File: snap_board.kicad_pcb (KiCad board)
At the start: 6 copper layers, 121 parts, among them U1 STM32MP157CAC3, U2 AS4C256M16D3LC-12BCN, U3 S40FC004C1B2C00000, U4 STPMIC1BPQR, U5 DF40C-70DP-0.4V(51), U6 DF40C-70DP-0.4V(51), U7 DF40C-70DP-0.4V(51), X1 32.768kHz, X2 24MHz

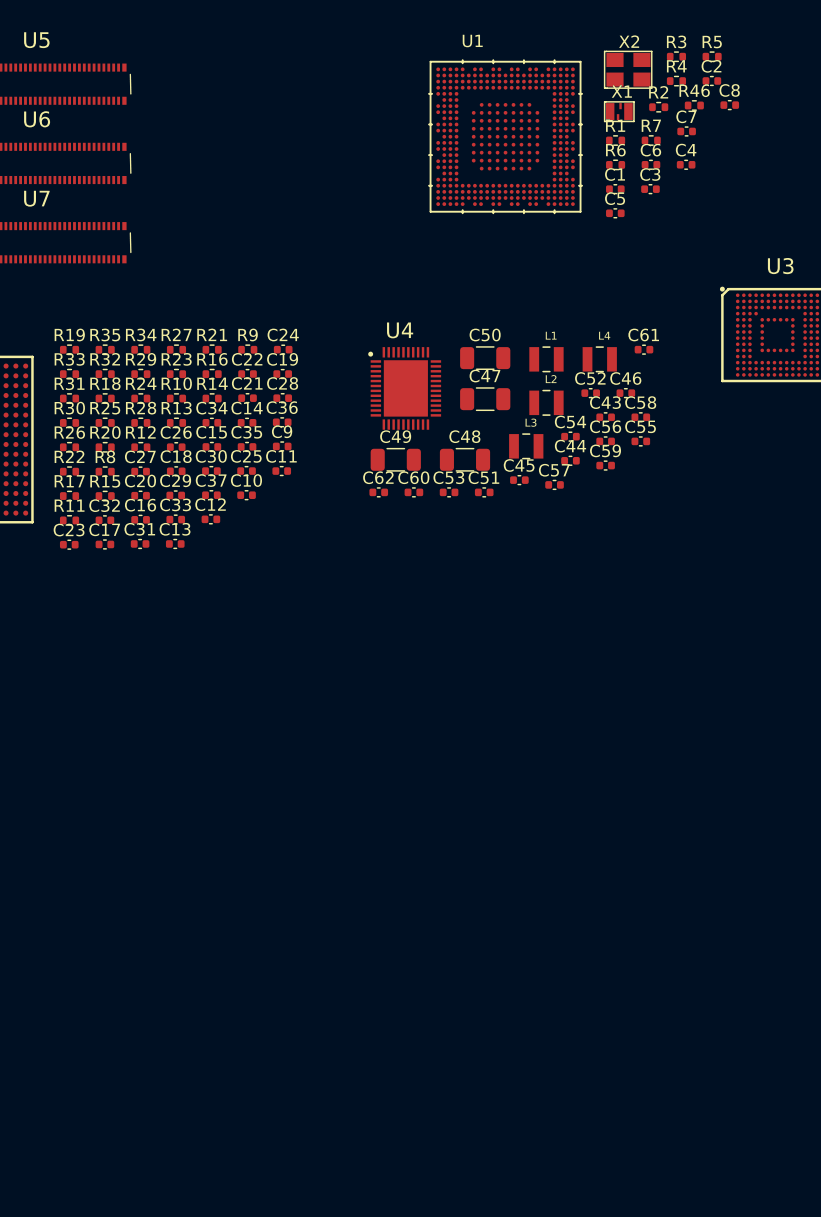
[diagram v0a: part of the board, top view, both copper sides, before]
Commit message: updated stm32 footprint
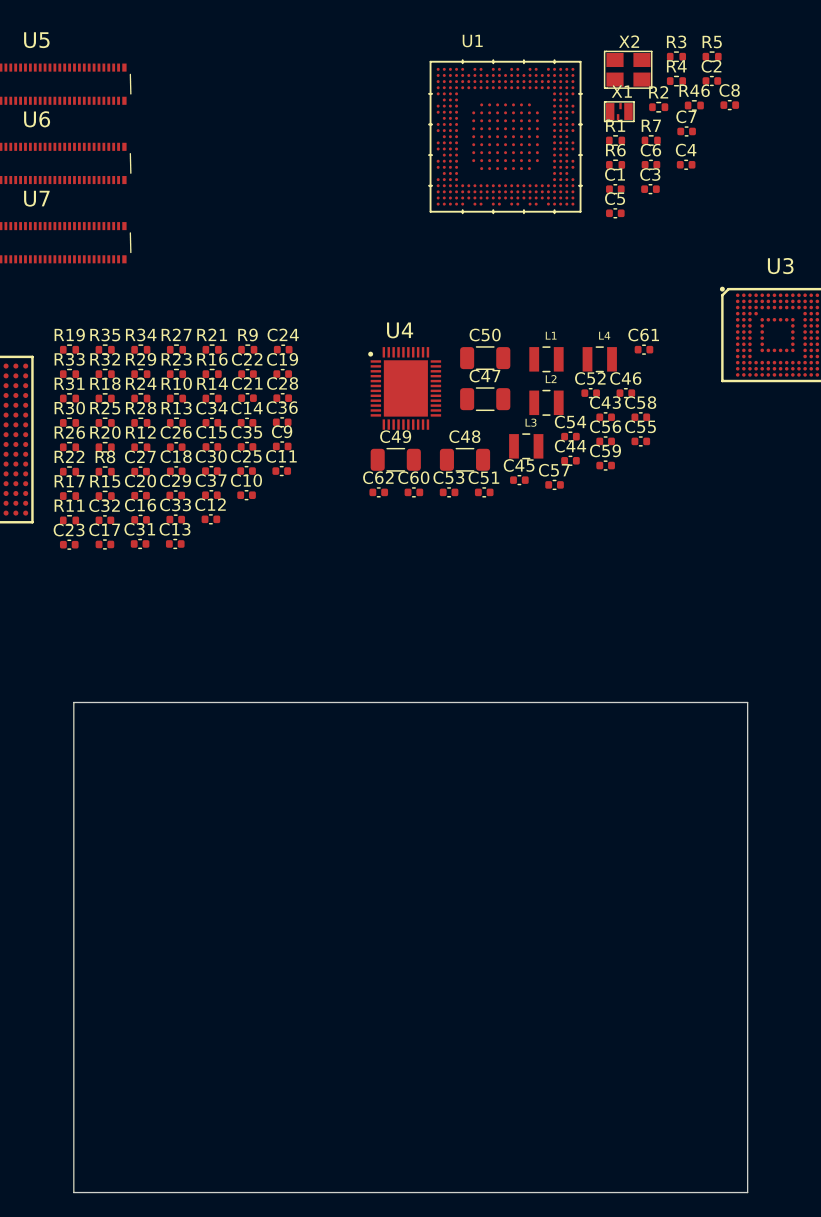
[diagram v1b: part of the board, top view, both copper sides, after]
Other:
- board outline added: 55 x 40 mm
- net class Default: clearance 0.2 -> 0.08; trace_width 0.25 -> 0.09; via_dia 0.8 -> 0.4; via_drill 0.4 -> 0.2
- rule trace_clearance: 0.2 -> 0.08
- rule trace_min: 0.2 -> 0.09
- rule via_min_drill: 0.3 -> 0.2

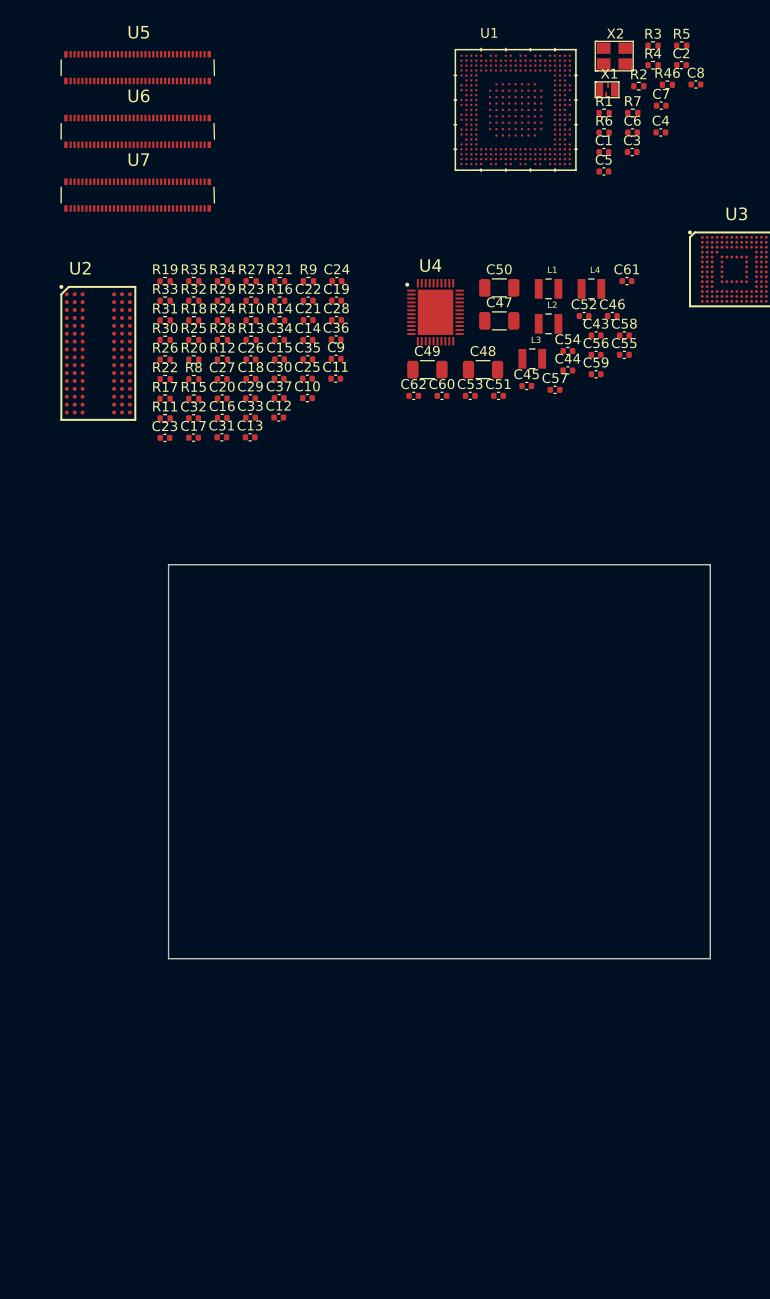
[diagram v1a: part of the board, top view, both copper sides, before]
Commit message: working on bga fanout
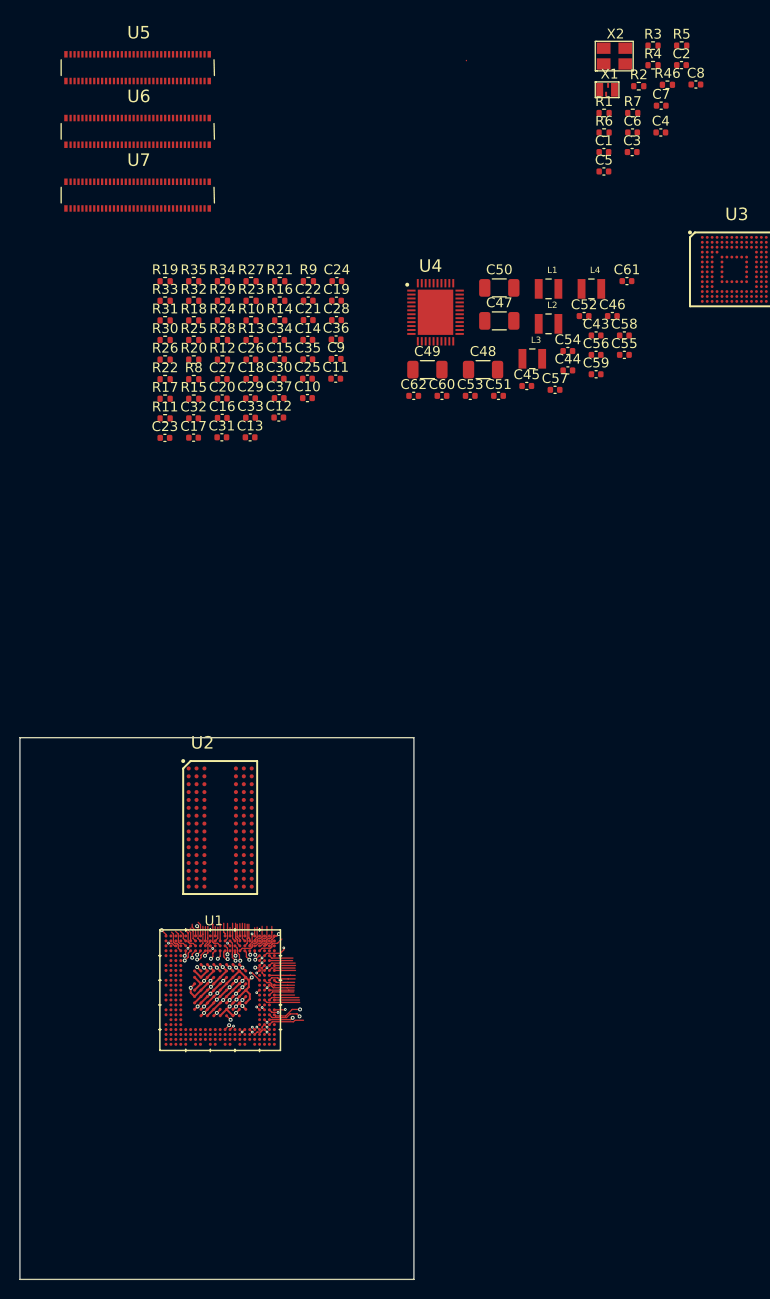
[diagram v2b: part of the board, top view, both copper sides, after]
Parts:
- moved U1 94.3 mm to (205.7, 148.6)
- moved U2 49.7 mm to (205.7, 132.1)
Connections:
- net DDR_DQS1N renamed DDR_DQS1_N
- net DDR_DQS1P renamed DDR_DQS1_P
- U1 pad 1E5: (no net) -> GND
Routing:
- net GND: track 0.00 -> 55.9 mm, vias 0 -> 19
- net PMIC_VOUT1_VDD_CORE: track 0.00 -> 18.3 mm, vias 0 -> 11
- net PMIC_VOUT3_VDD: track 0.00 -> 8.86 mm, vias 0 -> 8
- net SDMMC1_D3: track 0.00 -> 4.19 mm
- net Net-(C5-Pad2): track 0.00 -> 3.65 mm, vias 0 -> 1
- net DDR_DQ14: track 0.00 -> 3.64 mm
- net DDR_DQS1_P: track 0.00 -> 3.44 mm, vias 0 -> 1
- net DDR_A1: track 0.00 -> 3.11 mm
- net DDR_DQS1_N: track 0.00 -> 3.03 mm, vias 0 -> 1
- net DDR_RESETN: track 0.00 -> 2.90 mm
- net JTMS_SWDIO: track 0.00 -> 2.84 mm
- net Net-(U1-PadC19): track 0.00 -> 2.84 mm
- net DDR_A3: track 0.00 -> 2.76 mm
- net DDR_DQS0_P: track 0.00 -> 2.72 mm
- net DDR_DQ6: track 0.00 -> 2.71 mm
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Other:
- board size 55 x 40 mm -> 40 x 55 mm
- net class DDR_DiffPairs added: clearance 0.08, trace_width 0.09, via_dia 0.4, via_drill 0.2

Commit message: working on PCB
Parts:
- moved C61 126.4 mm to (141.3, 145.9), turned to 180 degrees
- moved C46 123.8 mm to (141.3, 146.9), turned to 180 degrees
- moved C58 120.4 mm to (141.4, 140.2), turned to 180 degrees
- moved C55 119.9 mm to (141.4, 141.2), turned to 180 degrees
- moved L4 119.0 mm to (147.0, 147.2), turned to 270 degrees
- moved C52 117.9 mm to (145.2, 146.5), turned to 270 degrees
- moved C56 117.7 mm to (144.1, 146.5), turned to 270 degrees
- moved C50 115.8 mm to (143.3, 149.2), turned to 180 degrees
- moved C54 114.0 mm to (141.4, 139.1), turned to 180 degrees
- moved C57 112.7 mm to (141.3, 142.6), turned to 180 degrees
- moved C44 112.5 mm to (141.4, 137.9), turned to 180 degrees
- moved C43 111.1 mm to (146.4, 135.4), turned to 90 degrees
- moved C45 111.0 mm to (141.3, 143.8), turned to 180 degrees
- moved L2 109.4 mm to (144.3, 135.5), turned to 90 degrees
- moved L1 107.6 mm to (148.9, 136.1)
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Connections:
- C57 pad 1: PMIC_LDO2_2V5 -> PMIC_LDO2_2V9
- U4 pad 11: PMIC_VOUT2_VDD_DDR -> Net-(L2-Pad1)
- U4 pad 5: Net-(L1-Pad1) -> PMIC_VOUT1_VDD_CORE
- U4 pad 7: PMIC_VOUT1_VDD_CORE -> Net-(L1-Pad1)
- U4 pad 9: Net-(L2-Pad1) -> PMIC_VOUT2_VDD_DDR
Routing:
- net GND: track 55.9 -> 82.4 mm, vias 19 -> 58
- net 5V_VIN: track 0.00 -> 11.1 mm, vias 0 -> 11
- net PMIC_VOUT2_VDD_DDR: track 1.84 -> 11.8 mm, vias 2 -> 10
- net PMIC_VOUT3_VDD: track 8.86 -> 16.9 mm, vias 8 -> 10
- net I2C4_SCL: track 0.00 -> 6.85 mm
- net I2C4_SDA: track 0.00 -> 6.10 mm
- net PMIC_WAKEUP: track 0.00 -> 5.54 mm
- net NRST: track 0.00 -> 5.31 mm
- net PMIC_LDO6_1V0: track 0.00 -> 4.89 mm
- net PMIC_LDO2_2V9: track 0.00 -> 4.82 mm, vias 0 -> 1
- net PMIC_LDO5: track 0.00 -> 4.33 mm
- net LCD_G5: track 0.00 -> 4.25 mm
- net PA0_WKUP: track 0.00 -> 4.21 mm
- net ETH_GTX_CLK: track 0.00 -> 4.18 mm
- net LCD_R0: track 0.00 -> 4.13 mm
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- added copper zone on F.Cu, net 5V_VIN
- added copper zone on F.Cu, net Net-(L1-Pad1)
- added copper zone on F.Cu, net Net-(L2-Pad1)
- added copper zone on F.Cu, net Net-(L3-Pad1)
- added copper zone on F.Cu, net Net-(L4-Pad1)
- added copper zone on F.Cu, net PMIC_LDO3_VTT_DDR
- added copper zone on F.Cu, net PMIC_VOUT1_VDD_CORE
- added copper zone on F.Cu, net PMIC_VOUT2_VDD_DDR
- added copper zone on F.Cu, net PMIC_VOUT3_VDD
- added copper zone on F.Cu, net PMIC_VOUT4_3V3

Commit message: working on RAM
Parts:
- R10, R11, R8, R9: moved to B.Cu
- moved R5 137.8 mm to (138.3, 129.7), turned to 270 degrees
- moved R46 135.5 mm to (138.3, 131.7), turned to 270 degrees
- moved R4 135.2 mm to (137.3, 129.7), turned to 270 degrees
- moved C59 116.8 mm to (137.9, 135.0)
- moved C51 107.4 mm to (137.9, 136.2)
- moved C62 98.6 mm to (137.9, 133.8)
- moved R9 77.5 mm to (143.7, 107.9), turned to 180 degrees
- moved R10 71.6 mm to (143.7, 110.2)
- moved R8 63.4 mm to (143.7, 109.0)
- moved U2 61.2 mm to (150.6, 105.4)
- moved U1 55.7 mm to (150.2, 152.6)
- moved R11 45.3 mm to (159.5, 110.5)
- moved C13 41.2 mm to (173.4, 113.5)
- moved C24 41.2 mm to (182.2, 97.7)
- moved C34 41.2 mm to (176.4, 103.7)
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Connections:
- C51 pad 1: PMIC_VOUT4_3V3 -> 5V_VIN
- U2 pad A2: DDR_DQ13 -> DDR_DQ0
- U2 pad A3: DDR_DQ15 -> DDR_DQ7
- U2 pad A7: DDR_DQ12 -> DDR_DQ2
- U2 pad B7: DDR_DQS1_P -> DDR_DQS0_N
- U2 pad B8: DDR_DQ14 -> DDR_DQ4
- U2 pad C2: DDR_DQ11 -> DDR_DQ3
- U2 pad C3: DDR_DQ9 -> DDR_DQ1
- U2 pad C7: DDR_DQS1_N -> DDR_DQS0_P
- U2 pad C8: DDR_DQ10 -> DDR_DQ5
- U2 pad D3: DDR_DQM1 -> DDR_DQM0
- U2 pad D7: DDR_DQ8 -> DDR_DQ6
- U2 pad E3: DDR_DQ0 -> DDR_DQ9
- U2 pad E7: DDR_DQM0 -> DDR_DQM1
- U2 pad F2: DDR_DQ2 -> DDR_DQ8
- U2 pad F3: DDR_DQS0_N -> DDR_DQS1_P
- U2 pad F7: DDR_DQ1 -> DDR_DQ11
- U2 pad F8: DDR_DQ3 -> DDR_DQ15
- U2 pad G2: DDR_DQ6 -> DDR_DQ10
- U2 pad G3: DDR_DQS0_P -> DDR_DQS1_N
- U2 pad H3: DDR_DQ4 -> DDR_DQ13
- U2 pad H7: DDR_DQ7 -> DDR_DQ14
- U2 pad H8: DDR_DQ5 -> DDR_DQ12
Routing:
- net GND: track 82.4 -> 104.8 mm, vias 58 -> 82
- net PMIC_VOUT2_VDD_DDR: track 11.8 -> 32.5 mm, vias 10 -> 22
- net PA0_WKUP: track 4.21 -> 8.31 mm
- net POWER_ON: track 2.07 -> 6.09 mm
- net PMIC_VOUT3_VDD: track 16.9 -> 20.6 mm, vias 10 -> 12
- net I2C4_SDA: track 6.10 -> 9.31 mm
- net PMIC_WAKEUP: track 5.54 -> 2.41 mm
- net PMIC_VREF_DDR: track 2.43 -> 5.26 mm, vias 0 -> 2
- net DDR_RESETN: track 3.36 -> 5.80 mm, vias 0 -> 1
- net Net-(C62-Pad1): track 0.00 -> 2.15 mm
- net I2C4_SCL: track 6.85 -> 8.82 mm
- net DDR_A13: track 1.20 -> 3.17 mm, vias 1 -> 2
- net DDR_A4: track 0.43 -> 2.07 mm, vias 1 -> 2
- net DDR_A8: track 2.90 -> 4.49 mm, vias 0 -> 1
- net DDR_A11: track 0.53 -> 2.09 mm, vias 1 -> 2
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- added copper zone on F.Cu, net PMIC_LDO4_VDD_USB
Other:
- board outline removed

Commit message: working on RAM
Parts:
- moved R1 128.7 mm to (147.8, 144.2), turned to 180 degrees
- moved R27 54.0 mm to (145.0, 143.6), turned to 180 degrees
- moved C24 47.4 mm to (156.9, 137.7), turned to 270 degrees
- moved C36 40.9 mm to (156.9, 135.7), turned to 90 degrees
- moved R34 38.5 mm to (156.8, 133.7), turned to 90 degrees
- moved C43 38.0 mm to (94.1, 129.1)
- moved C47 38.0 mm to (96.9, 127.2)
- moved C50 38.0 mm to (90.9, 142.9)
- moved L1 38.0 mm to (96.6, 129.9)
- moved R4 38.0 mm to (99.3, 130.2)
- moved R46 38.0 mm to (100.4, 132.1)
- moved C44 38.0 mm to (89.0, 131.7)
- moved C45 38.0 mm to (89.0, 137.6)
- moved C46 38.0 mm to (89.0, 140.7)
- moved C48 38.0 mm to (88.2, 128.4)
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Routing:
- net DDR_DQ12: track 0.83 -> 25.4 mm
- net DDR_DQS1_P: track 1.89 -> 26.0 mm
- net DDR_DQS1_N: track 1.29 -> 25.1 mm
- net DDR_DQM1: track 1.78 -> 24.9 mm
- net DDR_DQ9: track 2.29 -> 25.0 mm
- net DDR_DQ11: track 2.84 -> 25.0 mm
- net DDR_DQ13: track 1.25 -> 23.1 mm
- net DDR_DQ15: track 2.84 -> 24.6 mm
- net DDR_DQ8: track 2.47 -> 24.2 mm
- net DDR_DQ10: track 1.80 -> 23.5 mm
- net DDR_DQ14: track 1.49 -> 22.8 mm
- net GND: track 104.8 -> 113.7 mm, vias 82 -> 84
- net DDR_CSN: track 2.31 -> 11.1 mm, vias 1 -> 2
- net DDR_CKE: track 4.79 -> 12.5 mm, vias 1 -> 2
- net PMIC_VOUT2_VDD_DDR: track 32.5 -> 39.7 mm
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
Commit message: still working on RAM
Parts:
- C10, C11, C12, C13, C14, C15, C16, C17, C18, C19, C20, C21, C22, C30, C31, C32, C33, C9, R12, R13, R14, R15, R17, R18, R19, R20, R21, R22, R23, R24, R25, R26, R28, R29, R30, R31, R32, R33, R35: moved to B.Cu
- Re: renamed from R16; moved to B.Cu
- moved R21 51.0 mm to (145.2, 138.1)
- moved C11 48.5 mm to (143.2, 136.5), turned to 180 degrees
- moved R9 48.4 mm to (158.5, 129.9)
- moved C10 46.3 mm to (143.2, 138.6), turned to 180 degrees
- moved C28 46.0 mm to (145.8, 129.7), turned to 270 degrees
- moved C14 44.7 mm to (143.2, 129.9), turned to 180 degrees
- moved Re 43.3 mm to (158.4, 139.0), turned to 180 degrees
- moved R10 42.9 mm to (145.2, 134.8)
- moved R13 42.9 mm to (145.2, 135.9)
- moved R23 42.6 mm to (145.2, 131.6)
- moved C19 42.6 mm to (160.5, 136.3)
- moved R8 42.0 mm to (145.2, 132.6)
- moved R14 40.5 mm to (158.4, 137.9), turned to 180 degrees
- moved C12 40.2 mm to (143.2, 134.3), turned to 180 degrees
- moved C35 40.2 mm to (145.8, 127.7), turned to 270 degrees
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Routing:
- net DDR_CASN: track 1.73 -> 22.7 mm
- net DDR_RASN: track 1.54 -> 22.3 mm
- net DDR_WEN: track 1.48 -> 20.5 mm
- net DDR_ODT: track 5.37 -> 23.3 mm
- net DDR_CSN: track 11.1 -> 22.0 mm
- net GND: track 113.7 -> 122.4 mm, vias 84 -> 85
- net PMIC_VOUT2_VDD_DDR: track 39.7 -> 45.6 mm
- net DDR_DQ8: track 24.2 -> 26.1 mm
- net DDR_DQ10: track 23.5 -> 25.4 mm
- net PMIC_VREF_DDR: track 6.68 -> 8.37 mm

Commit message: still working on RAM
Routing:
- net DDR_A12: track 2.06 -> 25.9 mm
- net DDR_CLK_P: track 3.33 -> 26.7 mm
- net DDR_CLK_N: track 2.94 -> 25.8 mm
- net DDR_A0: track 1.58 -> 24.3 mm
- net DDR_A3: track 2.31 -> 24.7 mm
- net DDR_A5: track 1.10 -> 23.5 mm
- net DDR_A9: track 2.22 -> 23.9 mm
- net DDR_A2: track 1.95 -> 23.4 mm
- net DDR_A1: track 2.80 -> 23.8 mm
- net DDR_A6: track 0.43 -> 21.4 mm, vias 1 -> 2
- net DDR_BA0: track 2.94 -> 23.6 mm
- net DDR_A11: track 2.09 -> 22.7 mm
- net DDR_A10: track 1.95 -> 22.3 mm
- net DDR_A14: track 3.18 -> 23.3 mm
- net DDR_BA1: track 2.37 -> 22.1 mm
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
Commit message: ram almost complete
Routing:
- net DDR_DQ6: track 2.09 -> 27.2 mm
- net DDR_DQ4: track 3.11 -> 27.3 mm
- net DDR_DQS0_N: track 2.46 -> 26.5 mm
- net DDR_DQS0_P: track 3.13 -> 27.1 mm
- net DDR_DQ5: track 2.75 -> 26.2 mm
- net DDR_DQ7: track 3.78 -> 26.9 mm
- net DDR_DQ2: track 3.46 -> 26.1 mm
- net DDR_DQ1: track 3.38 -> 25.3 mm
- net DDR_DQ0: track 3.54 -> 25.1 mm
- net DDR_DQ3: track 3.50 -> 24.7 mm
- net DDR_DQM0: track 4.65 -> 25.6 mm
- net DDR_A14: track 23.3 -> 34.8 mm
- net DDR_A1: track 23.8 -> 35.1 mm
- net DDR_A11: track 22.7 -> 32.9 mm
- net DDR_WEN: track 20.2 -> 29.2 mm
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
